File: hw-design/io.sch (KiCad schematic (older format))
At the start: 12 parts, among them P1 CONN_01X02, P2 CONN_01X03, SW1 SP3T

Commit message: ERC passing
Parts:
- renumbered C9 to C17, C15 to C18, P1 to P3, P2 to P4, R18 to R29, R24 to R30, R25 to R31, R28 to R32, R17 to R33, R19 to R34, R23 to R35
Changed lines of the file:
@@
 	5600 2400 5600 2500
 $Comp
-L R R17
+L R R33
 U 1 1 54CBEC23
 P 6850 1850
-F 0 "R17" V 6900 2100 40  0000 C CNN
+F 0 "R33" V 6900 2100 40  0000 C CNN
 F 1 "10k" V 6857 1851 40  0000 C CNN
 F 2 "MOD_Footprints_Lib:SM0603" V 6780 1850 30  0001 C CNN
@@
 $EndComp
 $Comp
-L R R19
+L R R34
 U 1 1 54CBEC30
 P 7000 1850
-F 0 "R19" V 7050 2100 40  0000 C CNN
+F 0 "R34" V 7050 2100 40  0000 C CNN
 F 1 "10k" V 7007 1851 40  0000 C CNN
 F 2 "MOD_Footprints_Lib:SM0603" V 6930 1850 30  0001 C CNN
@@
 $EndComp
 $Comp
-L R R23
+L R R35
 U 1 1 54CBEC37
 P 7150 1850
-F 0 "R23" V 7200 2100 40  0000 C CNN
+F 0 "R35" V 7200 2100 40  0000 C CNN
 F 1 "10k" V 7157 1851 40  0000 C CNN
 F 2 "MOD_Footprints_Lib:SM0603" V 7080 1850 30  0001 C CNN
@@
 Connection ~ 7150 2600
 $Comp
-L R R18
+L R R29
 U 1 1 54CBEC53
 P 2050 1800
-F 0 "R18" V 2130 1800 40  0000 C CNN
+F 0 "R29" V 2130 1800 40  0000 C CNN
 F 1 "10k" V 2057 1801 40  0000 C CNN
 F 2 "MOD_Footprints_Lib:SM0603" V 1980 1800 30  0001 C CNN
@@
 SW3
 $Comp
-L R R24
+L R R30
 U 1 1 54CBEC6F
 P 3900 1700
-F 0 "R24" V 3980 1700 40  0000 C CNN
+F 0 "R30" V 3980 1700 40  0000 C CNN
 F 1 "100R" V 3907 1701 40  0000 C CNN
 F 2 "MOD_Footprints_Lib:SM0603" V 3830 1700 30  0001 C CNN
@@
 	3900 2050 3900 1950
 $Comp
-L R R25
+L R R31
 U 1 1 54CBEC82
 P 3900 2600
-F 0 "R25" V 3980 2600 40  0000 C CNN
+F 0 "R31" V 3980 2600 40  0000 C CNN
 F 1 "100R" V 3907 2601 40  0000 C CNN
 F 2 "MOD_Footprints_Lib:SM0603" V 3830 2600 30  0001 C CNN
@@
 $EndComp
 $Comp
-L R R28
+L R R32
 U 1 1 54CBEC89
 P 4150 2150
-F 0 "R28" V 4230 2150 40  0000 C CNN
+F 0 "R32" V 4230 2150 40  0000 C CNN
 F 1 "100R" V 4157 2151 40  0000 C CNN
 F 2 "MOD_Footprints_Lib:SM0603" V 4080 2150 30  0001 C CNN
@@
 	4400 2150 4700 2150
 $Comp
-L C C15
+L C C18
 U 1 1 54CBEC99
 P 4500 2450
-F 0 "C15" V 4350 2400 40  0000 L CNN
+F 0 "C18" V 4350 2400 40  0000 L CNN
 F 1 "100nF X7R" V 4650 2250 40  0000 L CNN
 F 2 "MOD_Footprints_Lib:SM0603" H 4538 2300 30  0001 C CNN
@@
 FOOT
 $Comp
-L C C9
+L C C17
 U 1 1 54CBECAC
 P 4300 1650
-F 0 "C9" V 4150 1600 40  0000 L CNN
+F 0 "C17" V 4150 1600 40  0000 L CNN
 F 1 "100nF X7R" V 4450 1450 40  0000 L CNN
 F 2 "MOD_Footprints_Lib:SM0603" H 4338 1500 30  0001 C CNN
@@
 $EndComp
 $Comp
-L GNDD #PWR?
+L GNDD #PWR060
 U 1 1 54E65047
 P 2050 2400
-F 0 "#PWR?" H 2050 2150 60  0001 C CNN
+F 0 "#PWR060" H 2050 2150 60  0001 C CNN
 F 1 "GNDD" H 2050 2250 60  0000 C CNN
 F 2 "" H 2050 2400 60  0000 C CNN
@@
 	2050 2250 2050 2400
 $Comp
-L +3.3VP #PWR?
+L +3.3VP #PWR061
 U 1 1 54E65255
 P 2050 1450
-F 0 "#PWR?" H 2100 1480 20  0001 C CNN
+F 0 "#PWR061" H 2100 1480 20  0001 C CNN
 F 1 "+3.3VP" H 2050 1540 30  0000 C CNN
 F 2 "" H 2050 1450 60  0000 C CNN
@@
 $EndComp
 $Comp
-L GNDD #PWR?
+L GNDD #PWR062
 U 1 1 54E661EA
 P 3900 2950
-F 0 "#PWR?" H 3900 2700 60  0001 C CNN
+F 0 "#PWR062" H 3900 2700 60  0001 C CNN
 F 1 "GNDD" H 3900 2800 60  0000 C CNN
 F 2 "" H 3900 2950 60  0000 C CNN
@@
 $EndComp
 $Comp
-L GNDD #PWR?
+L GNDD #PWR063
 U 1 1 54E665CD
 P 4500 2750
-F 0 "#PWR?" H 4500 2500 60  0001 C CNN
+F 0 "#PWR063" H 4500 2500 60  0001 C CNN
 F 1 "GNDD" H 4500 2600 60  0000 C CNN
 F 2 "" H 4500 2750 60  0000 C CNN
@@
 $EndComp
 $Comp
-L +3.3VP #PWR?
+L +3.3VP #PWR064
 U 1 1 54E66A75
 P 3900 1300
-F 0 "#PWR?" H 3950 1330 20  0001 C CNN
+F 0 "#PWR064" H 3950 1330 20  0001 C CNN
 F 1 "+3.3VP" H 3900 1390 30  0000 C CNN
 F 2 "" H 3900 1300 60  0000 C CNN
@@
 Connection ~ 3900 1350
 $Comp
-L GNDD #PWR?
+L GNDD #PWR065
 U 1 1 54E66D8A
 P 4300 1850
-F 0 "#PWR?" H 4300 1600 60  0001 C CNN
+F 0 "#PWR065" H 4300 1600 60  0001 C CNN
 F 1 "GNDD" H 4300 1700 60  0000 C CNN
 F 2 "" H 4300 1850 60  0000 C CNN
@@
 $EndComp
 $Comp
-L +3.3VP #PWR?
+L +3.3VP #PWR066
 U 1 1 54E69C36
 P 7000 1400
-F 0 "#PWR?" H 7050 1430 20  0001 C CNN
+F 0 "#PWR066" H 7050 1430 20  0001 C CNN
 F 1 "+3.3VP" H 7000 1490 30  0000 C CNN
 F 2 "" H 7000 1400 60  0000 C CNN
@@
 $EndComp
 $Comp
-L CONN_01X02 P1
+L CONN_01X02 P3
 U 1 1 54E6B5CA
 P 1750 2200
-F 0 "P1" H 1750 2350 50  0000 C CNN
+F 0 "P3" H 1750 2350 50  0000 C CNN
 F 1 "CONN_01X02" V 1850 2200 50  0000 C CNN
 F 2 "" H 1750 2200 60  0000 C CNN
@@
 $EndComp
 $Comp
-L CONN_01X03 P2
+L CONN_01X03 P4
 U 1 1 54E6CA4C
 P 3600 2150
-F 0 "P2" H 3600 2350 50  0000 C CNN
+F 0 "P4" H 3600 2350 50  0000 C CNN
 F 1 "CONN_01X03" V 3700 2150 50  0000 C CNN
 F 2 "" H 3600 2150 60  0000 C CNN
@@
 $EndComp
 $Comp
-L GNDD #PWR?
+L GNDD #PWR067
 U 1 1 54E753B2
 P 5600 2500
-F 0 "#PWR?" H 5600 2250 60  0001 C CNN
+F 0 "#PWR067" H 5600 2250 60  0001 C CNN
 F 1 "GNDD" H 5600 2350 60  0000 C CNN
 F 2 "" H 5600 2500 60  0000 C CNN

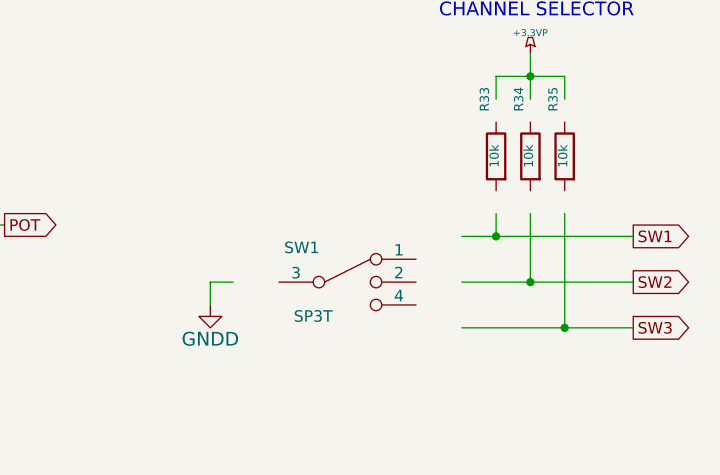
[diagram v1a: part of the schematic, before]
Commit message: wip: footprint association using default kicad libraries
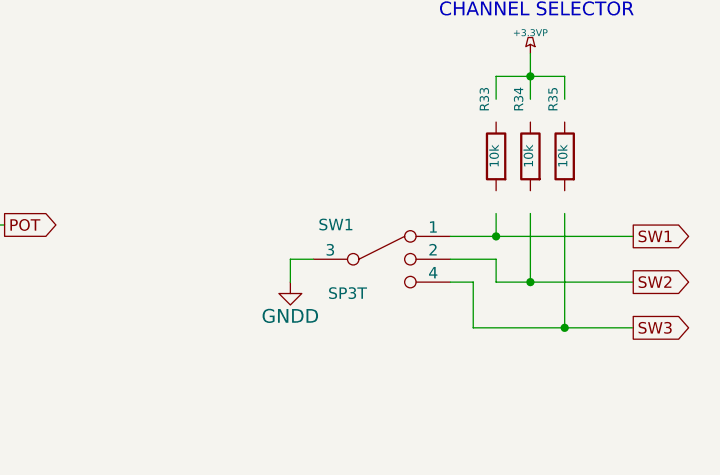
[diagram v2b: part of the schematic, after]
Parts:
- C17, C18: footprint MOD_Footprints_Lib:SM0603 -> Capacitors_SMD:C_0603
- P3: footprint (none) -> Pin_Headers:Pin_Header_Straight_1x02
- P4: footprint (none) -> Pin_Headers:Pin_Header_Straight_1x03
- R29, R30, R31, R32, R33, R34, R35: footprint MOD_Footprints_Lib:SM0603 -> Resistors_SMD:R_0603
- SW1: footprint (none) -> MOD_Footprints:SWITCH_HH_SK-13D26-G-6_5-K-GY
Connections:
- wire segments 29 -> 33
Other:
- moved on the sheet: SW1
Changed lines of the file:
@@
 Comment4 ""
 $EndDescr
-Wire Wire Line
-	5700 2400 5600 2400
-Wire Wire Line
-	5600 2400 5600 2500
 $Comp
 L R R33
@@
 F 0 "R33" V 6900 2100 40  0000 C CNN
 F 1 "10k" V 6857 1851 40  0000 C CNN
-F 2 "MOD_Footprints_Lib:SM0603" V 6780 1850 30  0001 C CNN
+F 2 "Resistors_SMD:R_0603" V 6780 1850 30  0001 C CNN
 F 3 "~" H 6850 1850 30  0000 C CNN
 	1    6850 1850
@@
 F 0 "R34" V 7050 2100 40  0000 C CNN
 F 1 "10k" V 7007 1851 40  0000 C CNN
-F 2 "MOD_Footprints_Lib:SM0603" V 6930 1850 30  0001 C CNN
+F 2 "Resistors_SMD:R_0603" V 6930 1850 30  0001 C CNN
 F 3 "~" H 7000 1850 30  0000 C CNN
 	1    7000 1850
@@
 F 0 "R35" V 7200 2100 40  0000 C CNN
 F 1 "10k" V 7157 1851 40  0000 C CNN
-F 2 "MOD_Footprints_Lib:SM0603" V 7080 1850 30  0001 C CNN
+F 2 "Resistors_SMD:R_0603" V 7080 1850 30  0001 C CNN
 F 3 "~" H 7150 1850 30  0000 C CNN
 	1    7150 1850
 	-1   0    0    -1
 $EndComp
-Wire Wire Line
-	7150 1500 7150 1600
-Wire Wire Line
-	6850 1500 7150 1500
-Wire Wire Line
-	6850 1500 6850 1600
-Wire Wire Line
-	7000 1400 7000 1600
-Connection ~ 7000 1500
-Wire Wire Line
-	6700 2200 7450 2200
-Wire Wire Line
-	6700 2400 7450 2400
-Wire Wire Line
-	6700 2600 7450 2600
-Wire Wire Line
-	6850 2100 6850 2200
-Connection ~ 6850 2200
-Wire Wire Line
-	7000 2100 7000 2400
-Connection ~ 7000 2400
-Wire Wire Line
-	7150 2100 7150 2600
-Connection ~ 7150 2600
 $Comp
 L R R29
@@
 F 0 "R29" V 2130 1800 40  0000 C CNN
 F 1 "10k" V 2057 1801 40  0000 C CNN
-F 2 "MOD_Footprints_Lib:SM0603" V 1980 1800 30  0001 C CNN
+F 2 "Resistors_SMD:R_0603" V 1980 1800 30  0001 C CNN
 F 3 "~" H 2050 1800 30  0000 C CNN
 	1    2050 1800
 	-1   0    0    -1
 $EndComp
-Wire Wire Line
-	2050 2250 1950 2250
-Wire Wire Line
-	2050 2050 2050 2150
-Wire Wire Line
-	1950 2150 2150 2150
-Wire Wire Line
-	2050 1450 2050 1550
 Text GLabel 2150 2150 2    50   Output ~ 0
 FOOT
-Connection ~ 2050 2150
 Text GLabel 7450 2200 2    50   Output ~ 0
 SW1
@@
 F 0 "R30" V 3980 1700 40  0000 C CNN
 F 1 "100R" V 3907 1701 40  0000 C CNN
-F 2 "MOD_Footprints_Lib:SM0603" V 3830 1700 30  0001 C CNN
+F 2 "Resistors_SMD:R_0603" V 3830 1700 30  0001 C CNN
 F 3 "~" H 3900 1700 30  0000 C CNN
 	1    3900 1700
 	1    0    0    1
 $EndComp
-Wire Wire Line
-	3900 2850 3900 2950
-Wire Wire Line
-	3800 2250 3900 2250
-Wire Wire Line
-	3900 2250 3900 2350
-Wire Wire Line
-	3800 2150 3900 2150
-Wire Wire Line
-	3800 2050 3900 2050
-Wire Wire Line
-	3900 2050 3900 1950
 $Comp
 L R R31
@@
 F 0 "R31" V 3980 2600 40  0000 C CNN
 F 1 "100R" V 3907 2601 40  0000 C CNN
-F 2 "MOD_Footprints_Lib:SM0603" V 3830 2600 30  0001 C CNN
+F 2 "Resistors_SMD:R_0603" V 3830 2600 30  0001 C CNN
 F 3 "~" H 3900 2600 30  0000 C CNN
 	1    3900 2600
@@
 F 0 "R32" V 4230 2150 40  0000 C CNN
 F 1 "100R" V 4157 2151 40  0000 C CNN
-F 2 "MOD_Footprints_Lib:SM0603" V 4080 2150 30  0001 C CNN
+F 2 "Resistors_SMD:R_0603" V 4080 2150 30  0001 C CNN
 F 3 "~" H 4150 2150 30  0000 C CNN
 	1    4150 2150
@@
 Text GLabel 4700 2150 2    50   Output ~ 0
 POT
-Wire Wire Line
-	4400 2150 4700 2150
 $Comp
 L C C18
@@
 F 0 "C18" V 4350 2400 40  0000 L CNN
 F 1 "100nF X7R" V 4650 2250 40  0000 L CNN
-F 2 "MOD_Footprints_Lib:SM0603" H 4538 2300 30  0001 C CNN
+F 2 "Capacitors_SMD:C_0603" H 4538 2300 30  0001 C CNN
 F 3 "~" H 4500 2450 60  0000 C CNN
 	1    4500 2450
 	-1   0    0    -1
 $EndComp
-Wire Wire Line
-	4500 2750 4500 2650
-Wire Wire Line
-	4500 2150 4500 2250
-Connection ~ 4500 2150
 Text Notes 3500 1150 0    60   ~ 0
 POTENCIOMETER 10K
@@
 F 0 "C17" V 4150 1600 40  0000 L CNN
 F 1 "100nF X7R" V 4450 1450 40  0000 L CNN
-F 2 "MOD_Footprints_Lib:SM0603" H 4338 1500 30  0001 C CNN
+F 2 "Capacitors_SMD:C_0603" H 4338 1500 30  0001 C CNN
 F 3 "~" H 4300 1650 60  0000 C CNN
 	1    4300 1650
@@
 	1    0    0    -1
 $EndComp
-Wire Wire Line
-	2050 2250 2050 2400
 $Comp
 L +3.3VP #PWR061
@@
 	1    0    0    -1
 $EndComp
-Wire Wire Line
-	3900 1300 3900 1450
-Wire Wire Line
-	4300 1450 4300 1350
-Wire Wire Line
-	4300 1350 3900 1350
-Connection ~ 3900 1350
 $Comp
 L GNDD #PWR065
@@
 F 0 "P3" H 1750 2350 50  0000 C CNN
 F 1 "CONN_01X02" V 1850 2200 50  0000 C CNN
-F 2 "" H 1750 2200 60  0000 C CNN
+F 2 "Pin_Headers:Pin_Header_Straight_1x02" H 1750 2200 60  0001 C CNN
 F 3 "" H 1750 2200 60  0000 C CNN
 	1    1750 2200
@@
 F 0 "P4" H 3600 2350 50  0000 C CNN
 F 1 "CONN_01X03" V 3700 2150 50  0000 C CNN
-F 2 "" H 3600 2150 60  0000 C CNN
+F 2 "Pin_Headers:Pin_Header_Straight_1x03" H 3600 2150 60  0001 C CNN
 F 3 "" H 3600 2150 60  0000 C CNN
 	1    3600 2150
@@
 L SP3T SW1
 U 1 1 54E74297
-P 6200 2400
-F 0 "SW1" H 6000 2550 50  0000 C CNN
-F 1 "SP3T" H 6050 2250 50  0000 C CNN
-F 2 "" H 6200 2400 60  0000 C CNN
-F 3 "" H 6200 2400 60  0000 C CNN
-	1    6200 2400
+P 6350 2300
+F 0 "SW1" H 6150 2450 50  0000 C CNN
+F 1 "SP3T" H 6200 2150 50  0000 C CNN
+F 2 "MOD_Footprints:SWITCH_HH_SK-13D26-G-6_5-K-GY" H 6350 2300 60  0001 C CNN
+F 3 "" H 6350 2300 60  0000 C CNN
+	1    6350 2300
 	1    0    0    -1
 $EndComp
@@
 L GNDD #PWR067
 U 1 1 54E753B2
-P 5600 2500
-F 0 "#PWR067" H 5600 2250 60  0001 C CNN
-F 1 "GNDD" H 5600 2350 60  0000 C CNN
-F 2 "" H 5600 2500 60  0000 C CNN
-F 3 "" H 5600 2500 60  0000 C CNN
-	1    5600 2500
-	1    0    0    -1
-$EndComp
+P 5950 2400
+F 0 "#PWR067" H 5950 2150 60  0001 C CNN
+F 1 "GNDD" H 5950 2250 60  0000 C CNN
+F 2 "" H 5950 2400 60  0000 C CNN
+F 3 "" H 5950 2400 60  0000 C CNN
+	1    5950 2400
+	1    0    0    -1
+$EndComp
+Wire Wire Line
+	6050 2300 5950 2300
+Wire Wire Line
+	5950 2300 5950 2400
+Wire Wire Line
+	7150 1500 7150 1600
+Wire Wire Line
+	6850 1500 7150 1500
+Wire Wire Line
+	6850 1500 6850 1600
+Wire Wire Line
+	7000 1400 7000 1600
+Connection ~ 7000 1500
+Wire Wire Line
+	6650 2200 7450 2200
+Wire Wire Line
+	6850 2400 7450 2400
+Wire Wire Line
+	6750 2600 7450 2600
+Wire Wire Line
+	6850 2100 6850 2200
+Connection ~ 6850 2200
+Wire Wire Line
+	7000 2100 7000 2400
+Connection ~ 7000 2400
+Wire Wire Line
+	7150 2100 7150 2600
+Connection ~ 7150 2600
+Wire Wire Line
+	2050 2250 1950 2250
+Wire Wire Line
+	2050 2050 2050 2150
+Wire Wire Line
+	1950 2150 2150 2150
+Wire Wire Line
+	2050 1450 2050 1550
+Connection ~ 2050 2150
+Wire Wire Line
+	3900 2850 3900 2950
+Wire Wire Line
+	3800 2250 3900 2250
+Wire Wire Line
+	3900 2250 3900 2350
+Wire Wire Line
+	3800 2150 3900 2150
+Wire Wire Line
+	3800 2050 3900 2050
+Wire Wire Line
+	3900 2050 3900 1950
+Wire Wire Line
+	4400 2150 4700 2150
+Wire Wire Line
+	4500 2750 4500 2650
+Wire Wire Line
+	4500 2150 4500 2250
+Connection ~ 4500 2150
+Wire Wire Line
+	2050 2250 2050 2400
+Wire Wire Line
+	3900 1300 3900 1450
+Wire Wire Line
+	4300 1450 4300 1350
+Wire Wire Line
+	4300 1350 3900 1350
+Connection ~ 3900 1350
+Wire Wire Line
+	6850 2400 6850 2300
+Wire Wire Line
+	6850 2300 6650 2300
+Wire Wire Line
+	6750 2600 6750 2400
+Wire Wire Line
+	6750 2400 6650 2400
 $EndSCHEMATC
